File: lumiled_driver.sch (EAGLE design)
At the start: 10 parts, among them IC1 LD117AV, X1 PWR

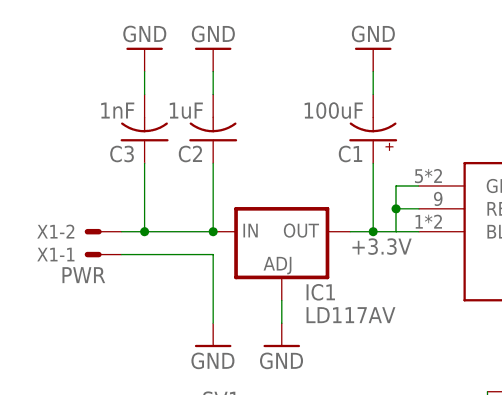
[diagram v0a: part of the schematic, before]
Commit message: -fixed a capacitor value -added screenshots of the board headers for the LED boards
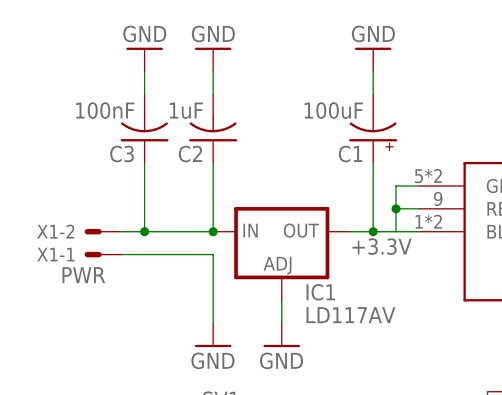
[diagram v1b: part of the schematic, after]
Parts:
- C3: value 1nF -> 100nF
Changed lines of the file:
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@@
 <grid distance="0.1" unitdist="inch" unit="inch" style="lines" multiple="1" display="no" altdistance="0.01" altunitdist="inch" altunit="inch"/>
 <layers>
-<layer number="1" name="Top" color="4" fill="1" visible="no" active="no"/>
-<layer number="2" name="Route2" color="1" fill="3" visible="no" active="no"/>
-<layer number="3" name="Route3" color="4" fill="3" visible="no" active="no"/>
-<layer number="4" name="Route4" color="1" fill="4" visible="no" active="no"/>
-<layer number="5" name="Route5" color="4" fill="4" visible="no" active="no"/>
-<layer number="6" name="Route6" color="1" fill="8" visible="no" active="no"/>
-<layer number="7" name="Route7" color="4" fill="8" visible="no" active="no"/>
-<layer number="8" name="Route8" color="1" fill="2" visible="no" active="no"/>
-<layer number="9" name="Route9" color="4" fill="2" visible="no" active="no"/>
-<layer number="10" name="Route10" color="1" fill="7" visible="no" active="no"/>
-<layer number="11" name="Route11" color="4" fill="7" visible="no" active="no"/>
-<layer number="12" name="Route12" color="1" fill="5" visible="no" active="no"/>
-<layer number="13" name="Route13" color="4" fill="5" visible="no" active="no"/>
-<layer number="14" name="Route14" color="1" fill="6" visible="no" active="no"/>
-<layer number="15" name="Route15" color="4" fill="6" visible="no" active="no"/>
-<layer number="16" name="Bottom" color="1" fill="1" visible="no" active="no"/>
-<layer number="17" name="Pads" color="2" fill="1" visible="no" active="no"/>
-<layer number="18" name="Vias" color="2" fill="1" visible="no" active="no"/>
-<layer number="19" name="Unrouted" color="6" fill="1" visible="no" active="no"/>
-<layer number="20" name="Dimension" color="24" fill="1" visible="no" active="no"/>
-<layer number="21" name="tPlace" color="7" fill="1" visible="no" active="no"/>
-<layer number="22" name="bPlace" color="7" fill="1" visible="no" active="no"/>
-<layer number="23" name="tOrigins" color="15" fill="1" visible="no" active="no"/>
-<layer number="24" name="bOrigins" color="15" fill="1" visible="no" active="no"/>
-<layer number="25" name="tNames" color="7" fill="1" visible="no" active="no"/>
-<layer number="26" name="bNames" color="7" fill="1" visible="no" active="no"/>
-<layer number="27" name="tValues" color="7" fill="1" visible="no" active="no"/>
-<layer number="28" name="bValues" color="7" fill="1" visible="no" active="no"/>
+<layer number="1" name="Top" color="4" fill="1" visible="yes" active="no"/>
+<layer number="2" name="Route2" color="1" fill="3" visible="yes" active="no"/>
+<layer number="3" name="Route3" color="4" fill="3" visible="yes" active="no"/>
+<layer number="4" name="Route4" color="1" fill="4" visible="yes" active="no"/>
+<layer number="5" name="Route5" color="4" fill="4" visible="yes" active="no"/>
+<layer number="6" name="Route6" color="1" fill="8" visible="yes" active="no"/>
+<layer number="7" name="Route7" color="4" fill="8" visible="yes" active="no"/>
+<layer number="8" name="Route8" color="1" fill="2" visible="yes" active="no"/>
+<layer number="9" name="Route9" color="4" fill="2" visible="yes" active="no"/>
+<layer number="10" name="Route10" color="1" fill="7" visible="yes" active="no"/>
+<layer number="11" name="Route11" color="4" fill="7" visible="yes" active="no"/>
+<layer number="12" name="Route12" color="1" fill="5" visible="yes" active="no"/>
+<layer number="13" name="Route13" color="4" fill="5" visible="yes" active="no"/>
+<layer number="14" name="Route14" color="1" fill="6" visible="yes" active="no"/>
+<layer number="15" name="Route15" color="4" fill="6" visible="yes" active="no"/>
+<layer number="16" name="Bottom" color="1" fill="1" visible="yes" active="no"/>
+<layer number="17" name="Pads" color="2" fill="1" visible="yes" active="no"/>
+<layer number="18" name="Vias" color="2" fill="1" visible="yes" active="no"/>
+<layer number="19" name="Unrouted" color="6" fill="1" visible="yes" active="no"/>
+<layer number="20" name="Dimension" color="24" fill="1" visible="yes" active="no"/>
+<layer number="21" name="tPlace" color="7" fill="1" visible="yes" active="no"/>
+<layer number="22" name="bPlace" color="7" fill="1" visible="yes" active="no"/>
+<layer number="23" name="tOrigins" color="15" fill="1" visible="yes" active="no"/>
+<layer number="24" name="bOrigins" color="15" fill="1" visible="yes" active="no"/>
+<layer number="25" name="tNames" color="7" fill="1" visible="yes" active="no"/>
+<layer number="26" name="bNames" color="7" fill="1" visible="yes" active="no"/>
+<layer number="27" name="tValues" color="7" fill="1" visible="yes" active="no"/>
+<layer number="28" name="bValues" color="7" fill="1" visible="yes" active="no"/>
 <layer number="29" name="tStop" color="7" fill="3" visible="no" active="no"/>
 <layer number="30" name="bStop" color="7" fill="6" visible="no" active="no"/>
@@
 <layer number="35" name="tGlue" color="7" fill="4" visible="no" active="no"/>
 <layer number="36" name="bGlue" color="7" fill="5" visible="no" active="no"/>
-<layer number="37" name="tTest" color="7" fill="1" visible="no" active="no"/>
-<layer number="38" name="bTest" color="7" fill="1" visible="no" active="no"/>
+<layer number="37" name="tTest" color="7" fill="1" visible="yes" active="no"/>
+<layer number="38" name="bTest" color="7" fill="1" visible="yes" active="no"/>
 <layer number="39" name="tKeepout" color="4" fill="11" visible="no" active="no"/>
 <layer number="40" name="bKeepout" color="1" fill="11" visible="no" active="no"/>
@@
 <layer number="44" name="Drills" color="7" fill="1" visible="no" active="no"/>
 <layer number="45" name="Holes" color="7" fill="1" visible="no" active="no"/>
-<layer number="46" name="Milling" color="3" fill="1" visible="no" active="no"/>
-<layer number="47" name="Measures" color="7" fill="1" visible="no" active="no"/>
-<layer number="48" name="Document" color="7" fill="1" visible="no" active="no"/>
-<layer number="49" name="Reference" color="7" fill="1" visible="no" active="no"/>
-<layer number="51" name="tDocu" color="7" fill="1" visible="no" active="no"/>
-<layer number="52" name="bDocu" color="7" fill="1" visible="no" active="no"/>
+<layer number="46" name="Milling" color="3" fill="1" visible="yes" active="no"/>
+<layer number="47" name="Measures" color="7" fill="1" visible="yes" active="no"/>
+<layer number="48" name="Document" color="7" fill="1" visible="yes" active="no"/>
+<layer number="49" name="Reference" color="7" fill="1" visible="yes" active="no"/>
+<layer number="51" name="tDocu" color="7" fill="1" visible="yes" active="no"/>
+<layer number="52" name="bDocu" color="7" fill="1" visible="yes" active="no"/>
 <layer number="88" name="SimResults" color="9" fill="1" visible="yes" active="yes"/>
 <layer number="89" name="SimProbes" color="9" fill="1" visible="yes" active="yes"/>
@@
 <part name="GND6" library="supply1" library_urn="urn:adsk.eagle:library:371" deviceset="GND" device=""/>
 <part name="C2" library="rcl" library_urn="urn:adsk.eagle:library:334" deviceset="C-US" device="025-024X044" package3d_urn="urn:adsk.eagle:package:23630/1" value="1uF"/>
-<part name="C3" library="rcl" library_urn="urn:adsk.eagle:library:334" deviceset="C-US" device="025-024X044" package3d_urn="urn:adsk.eagle:package:23630/1" value="1nF"/>
+<part name="C3" library="rcl" library_urn="urn:adsk.eagle:library:334" deviceset="C-US" device="025-024X044" package3d_urn="urn:adsk.eagle:package:23630/1" value="100nF"/>
 <part name="GND7" library="supply1" library_urn="urn:adsk.eagle:library:371" deviceset="GND" device=""/>
 <part name="GND8" library="supply1" library_urn="urn:adsk.eagle:library:371" deviceset="GND" device=""/>
